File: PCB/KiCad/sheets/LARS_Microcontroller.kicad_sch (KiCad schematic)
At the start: 31 parts, among them J1 Reset Header, J2 SWD Flash, SW1 Reset, U1 STM32F429ZIT6TR, Y1 IQXO-791 8.00MHz

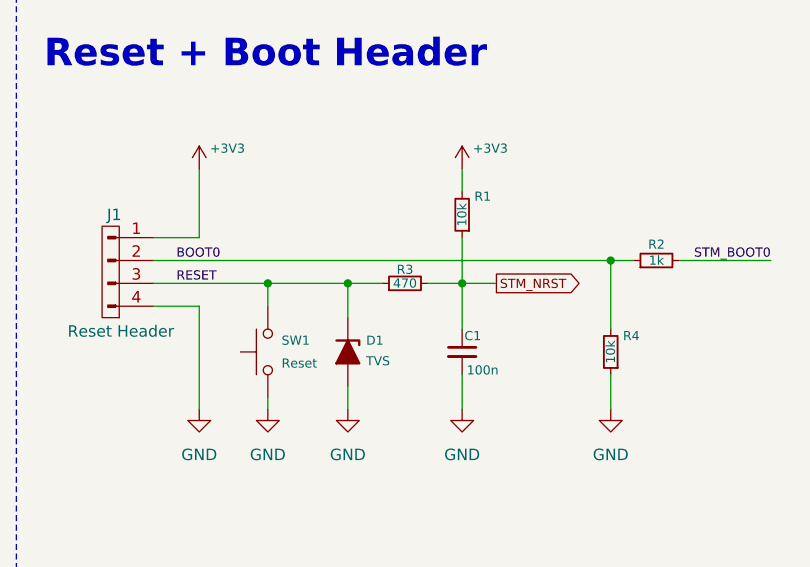
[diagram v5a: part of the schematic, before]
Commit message: PCB: update resistor values and embed font
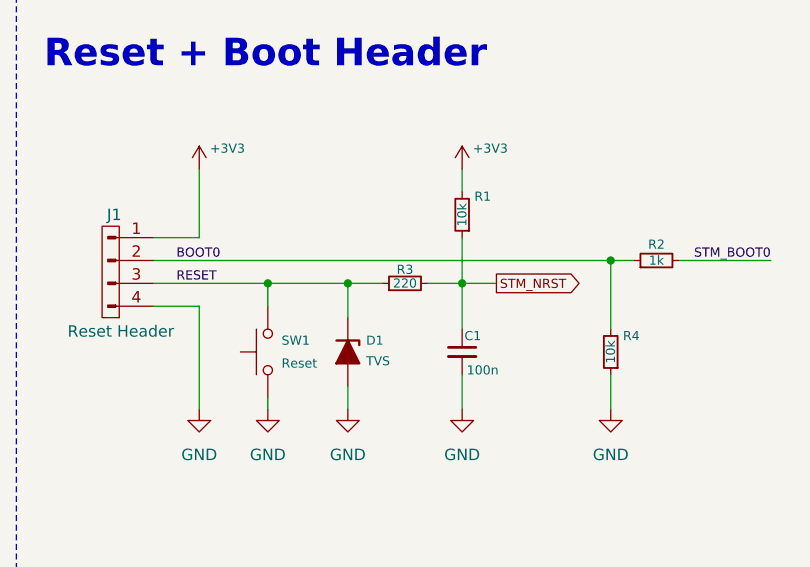
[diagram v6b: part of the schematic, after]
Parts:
- R3: value 470 -> 220
